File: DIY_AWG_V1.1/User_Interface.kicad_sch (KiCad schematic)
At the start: 29 parts, among them SW10 SW_Push, SW11 SW_Push, SW12 SW_Push, SW13 SW_Push, SW14 SW_Push, SW15 SW_Push, SW16 SW_Push, SW17 SW_Push, SW18 SW_Push, SW19 SW_Push, SW20 SW_Push, SW21 SW_Push, SW22 SW_Push, SW23 SW_Push, SW3 SW_Push, SW4 SW_Push, SW5 SW_Push, SW6 SW_Push, SW7 SW_Push, SW8 SW_Push, SW9 SW_Push, U14 EC12D1564402, U15 EC12E2430404

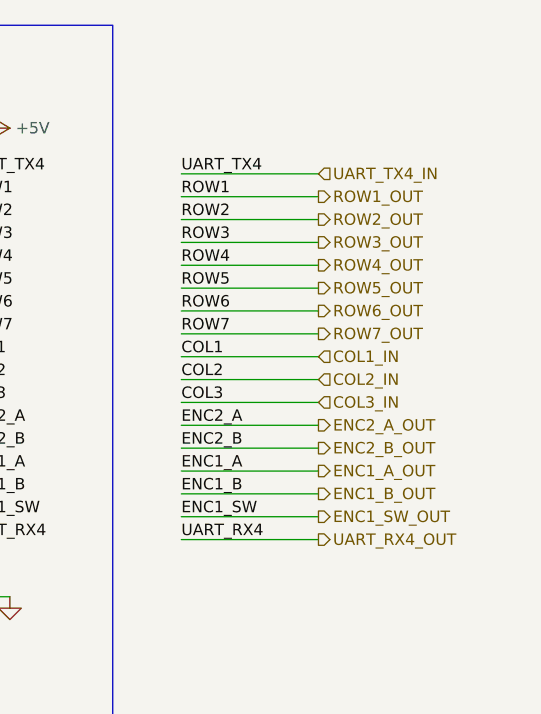
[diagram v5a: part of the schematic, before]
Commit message: Updated schematics to clear ERCs
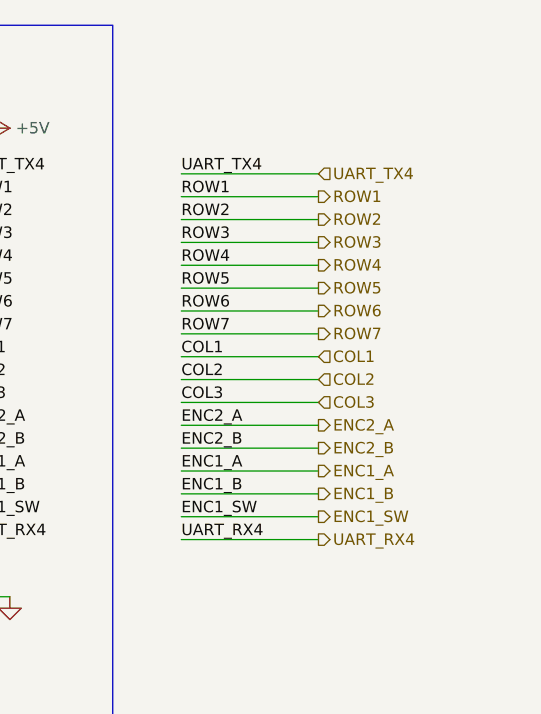
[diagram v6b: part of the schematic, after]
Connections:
- net COL1_IN renamed COL1
- net COL2_IN renamed COL2
- net COL3_IN renamed COL3
- net ENC1_A_OUT renamed ENC1_A
- net ENC1_B_OUT renamed ENC1_B
- net ENC1_SW_OUT renamed ENC1_SW
- net ENC2_A_OUT renamed ENC2_A
- net ENC2_B_OUT renamed ENC2_B
- net ROW1_OUT renamed ROW1
- net ROW2_OUT renamed ROW2
- net ROW3_OUT renamed ROW3
- net ROW4_OUT renamed ROW4
- net ROW5_OUT renamed ROW5
- net ROW6_OUT renamed ROW6
- net ROW7_OUT renamed ROW7
- net UART_RX4_OUT renamed UART_RX4
- net UART_TX4_IN renamed UART_TX4
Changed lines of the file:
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@@
 		)
 	)
-	(hierarchical_label "ROW6_OUT"
+	(hierarchical_label "ROW6"
 		(shape output)
 		(at 196.85 128.27 0)
@@
 		)
 	)
-	(hierarchical_label "ENC1_B_OUT"
+	(hierarchical_label "ENC1_B"
 		(shape output)
 		(at 196.85 148.59 0)
@@
 		)
 	)
-	(hierarchical_label "COL1_IN"
+	(hierarchical_label "COL1"
 		(shape input)
 		(at 196.85 133.35 0)
@@
 		)
 	)
-	(hierarchical_label "ROW5_OUT"
+	(hierarchical_label "ROW5"
 		(shape output)
 		(at 196.85 125.73 0)
@@
 		)
 	)
-	(hierarchical_label "ROW7_OUT"
+	(hierarchical_label "ROW7"
 		(shape output)
 		(at 196.85 130.81 0)
@@
 		)
 	)
-	(hierarchical_label "ROW1_OUT"
+	(hierarchical_label "ROW1"
 		(shape output)
 		(at 196.85 115.57 0)
@@
 		)
 	)
-	(hierarchical_label "ENC1_SW_OUT"
+	(hierarchical_label "ENC1_SW"
 		(shape output)
 		(at 196.85 151.13 0)
@@
 		)
 	)
-	(hierarchical_label "UART_RX4_OUT"
+	(hierarchical_label "UART_RX4"
 		(shape output)
 		(at 196.85 153.67 0)
@@
 		)
 	)
-	(hierarchical_label "ROW4_OUT"
+	(hierarchical_label "ROW4"
 		(shape output)
 		(at 196.85 123.19 0)
@@
 		)
 	)
-	(hierarchical_label "ROW2_OUT"
+	(hierarchical_label "ROW2"
 		(shape output)
 		(at 196.85 118.11 0)
@@
 		)
 	)
-	(hierarchical_label "UART_TX4_IN"
+	(hierarchical_label "UART_TX4"
 		(shape input)
 		(at 196.85 113.03 0)
@@
 		)
 	)
-	(hierarchical_label "ENC2_B_OUT"
+	(hierarchical_label "ENC2_B"
 		(shape output)
 		(at 196.85 143.51 0)
@@
 		)
 	)
-	(hierarchical_label "COL2_IN"
+	(hierarchical_label "COL2"
 		(shape input)
 		(at 196.85 135.89 0)
@@
 		)
 	)
-	(hierarchical_label "ROW3_OUT"
+	(hierarchical_label "ROW3"
 		(shape output)
 		(at 196.85 120.65 0)
@@
 		)
 	)
-	(hierarchical_label "COL3_IN"
+	(hierarchical_label "COL3"
 		(shape input)
 		(at 196.85 138.43 0)
@@
 		)
 	)
-	(hierarchical_label "ENC1_A_OUT"
+	(hierarchical_label "ENC1_A"
 		(shape output)
 		(at 196.85 146.05 0)
@@
 		)
 	)
-	(hierarchical_label "ENC2_A_OUT"
+	(hierarchical_label "ENC2_A"
 		(shape output)
 		(at 196.85 140.97 0)

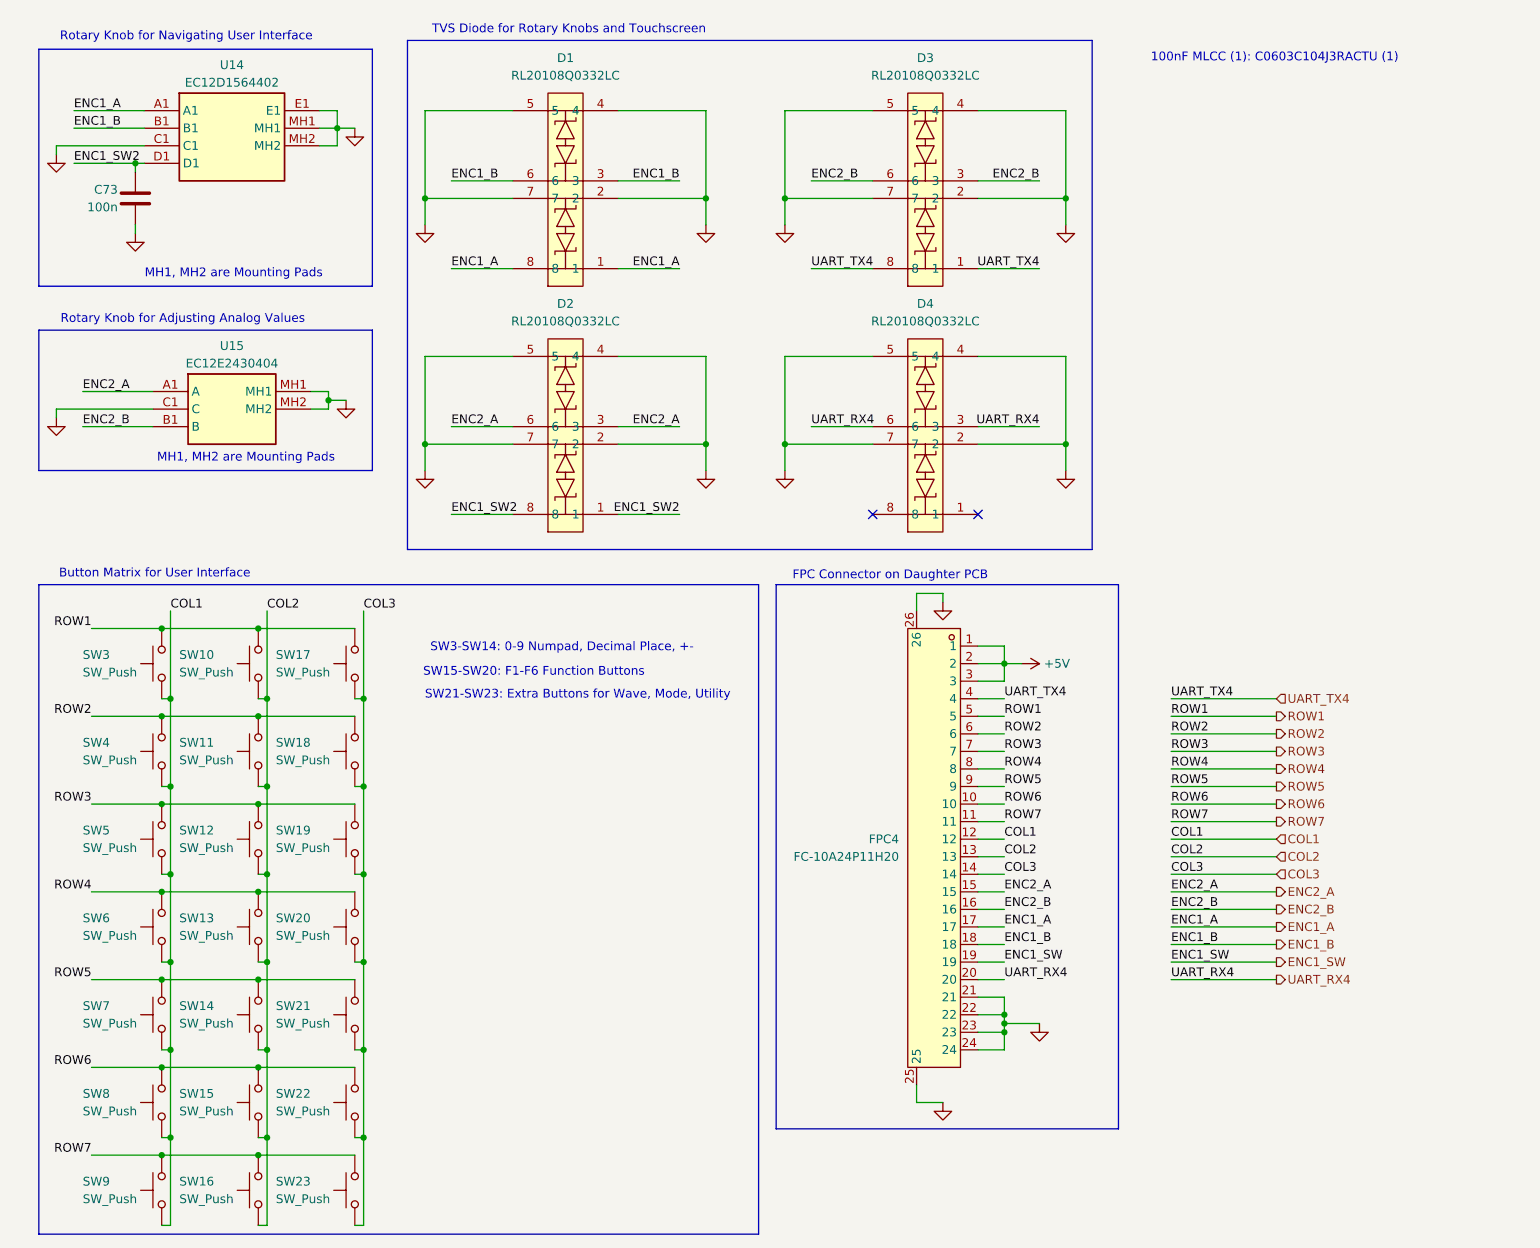
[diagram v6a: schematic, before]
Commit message: Updated the schematics to resolve ERCs
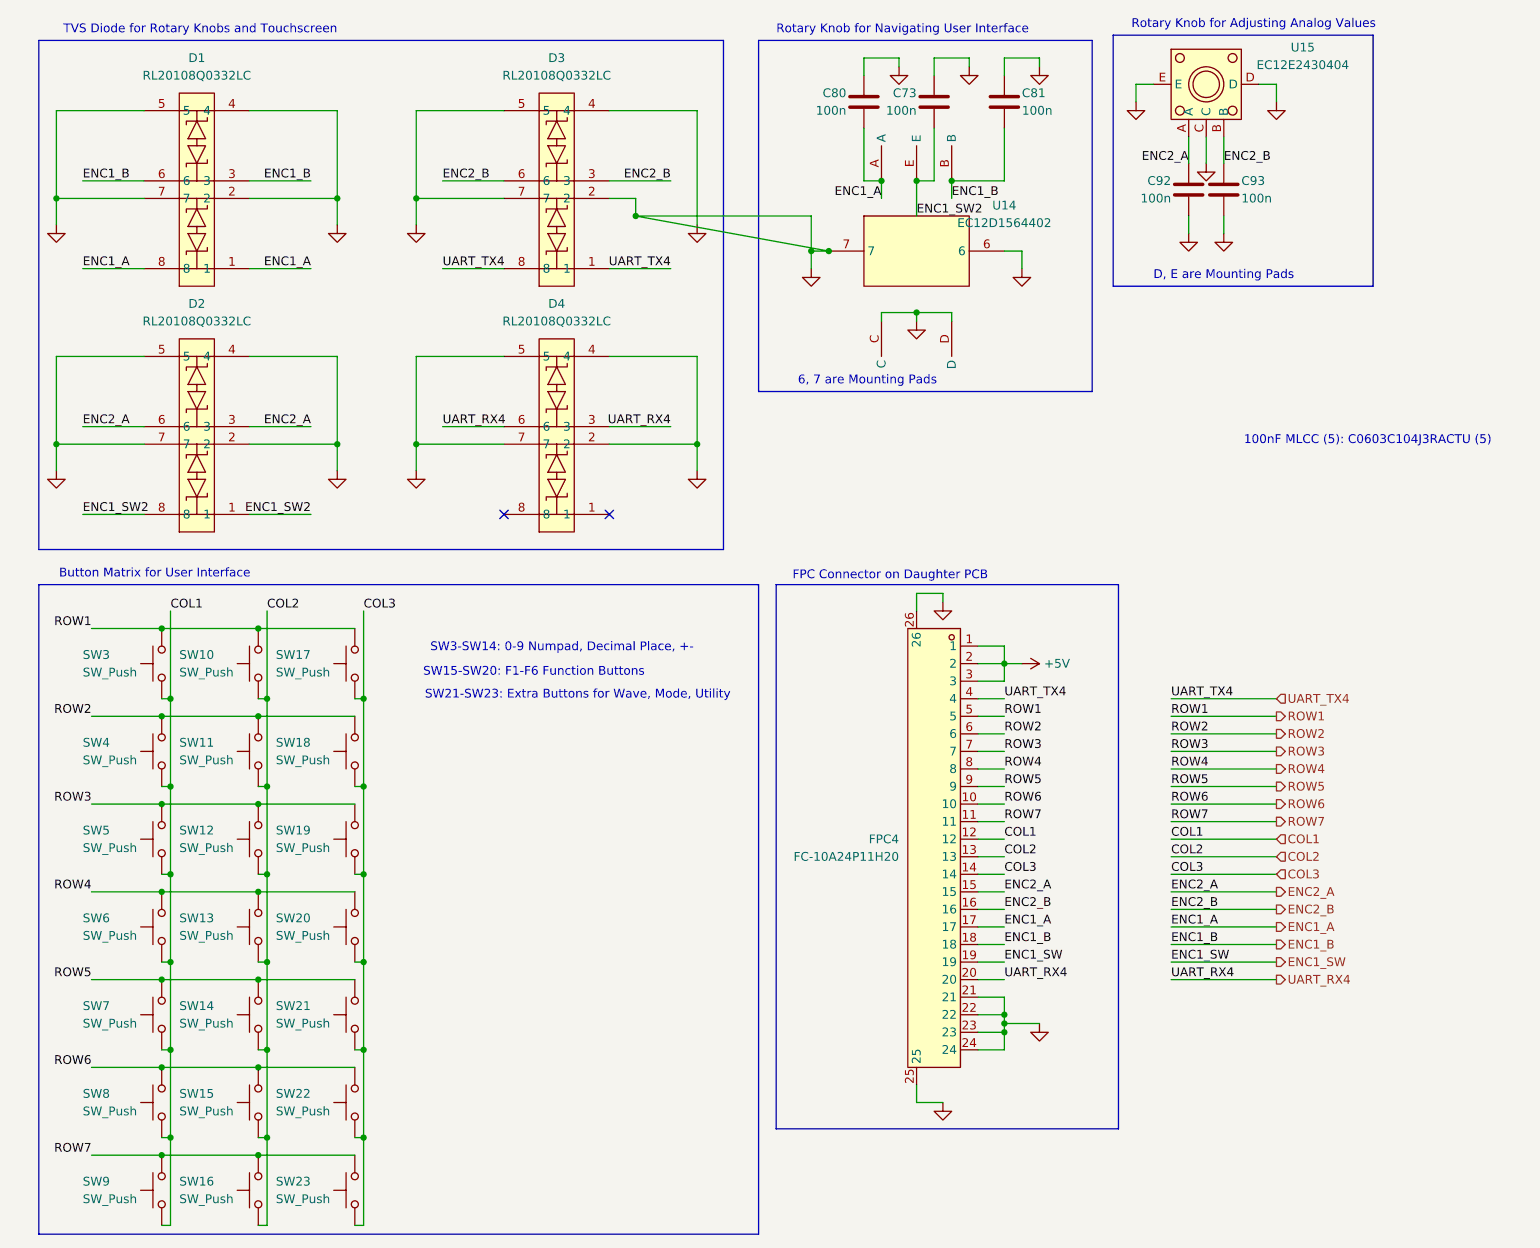
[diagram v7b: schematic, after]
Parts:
- removed U14: EC12D1564402, EC12D1564402, symbol EC12D1564402:EC12D1564402
- removed U15: EC12E2430404, EC12E2430404, symbol EC12E2430404:EC12E2430404
- added C80, C81, C92, C93: 100n, symbol Device:C
- added U14: EC12D1564402, easyeda2kicad:SW-TH_EC12D1564402, symbol easyeda2kicad:EC12D1564402
- added U15: EC12E2430404, easyeda2kicad:SW-TH_ALPSALPINE_EC12EXXXX, symbol easyeda2kicad:EC12E2430404
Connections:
- net ENC1_A: now also C80.2, U14.A
- net ENC1_B: now also C81.2, U14.B
- net ENC1_SW2: now also C73.2, U14.E; no longer C73.1
- net ENC2_A: now also C92.1, U15.A
- net ENC2_B: now also C93.1, U15.B
- net GND: now also C73.1, C80.1, C81.1, C92.2, C93.2, U14.6, U14.7, U14.C, U14.D, U15.C, U15.D, U15.E; no longer C73.2
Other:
- note added: "100nF MLCC (5): C0603C104J3RACTU (5)"
- note added: "6, 7 are Mounting Pads"
- note added: "D, E are Mounting Pads"
- note removed: "100nF MLCC (1): C0603C104J3RACTU (1)"
- note removed: "MH1, MH2 are Mounting Pads"
- moved on the sheet: D1, D2, D3, D4
